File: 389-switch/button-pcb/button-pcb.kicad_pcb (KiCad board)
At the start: 2 copper layers, 17.4 x 17.4 mm, 6 parts, among them J1 Conn_01x04, SW1 SW_DIP_x01

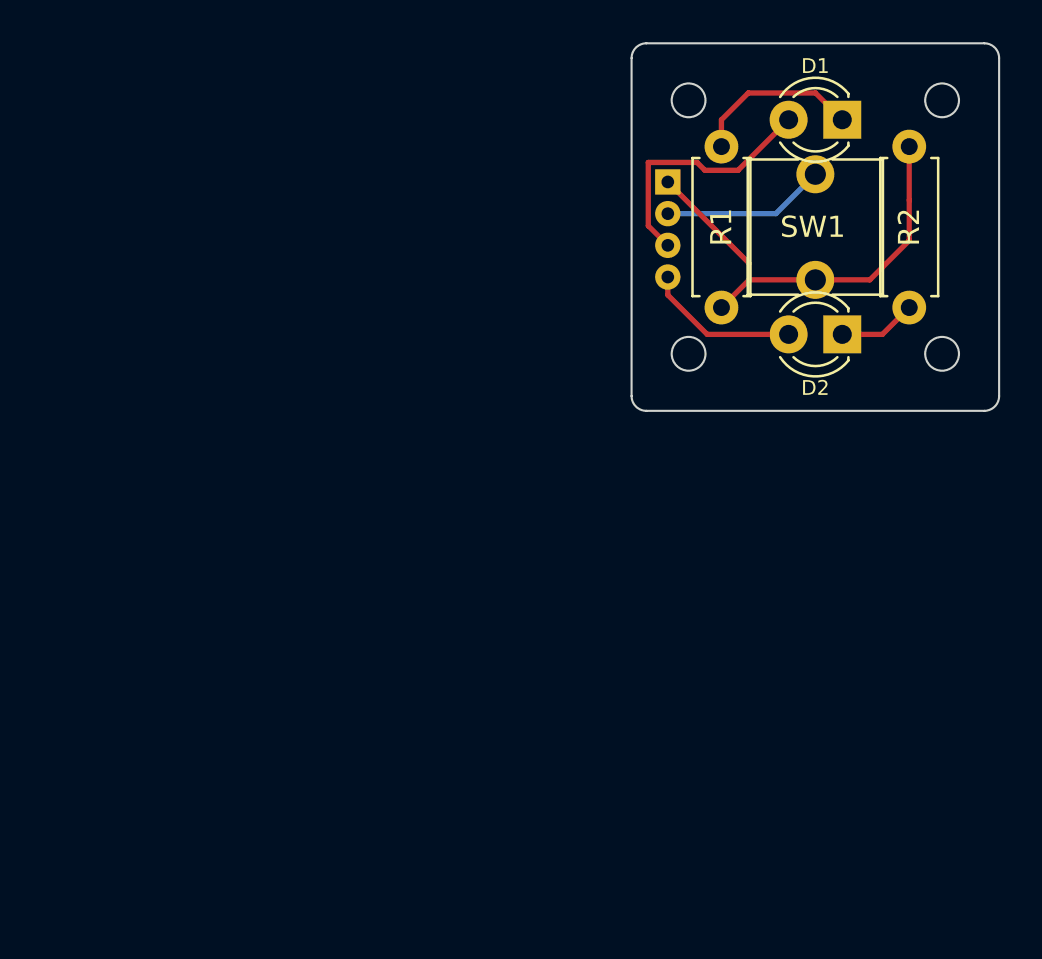
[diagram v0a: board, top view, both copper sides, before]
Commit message: changing pcb and creating gerber files
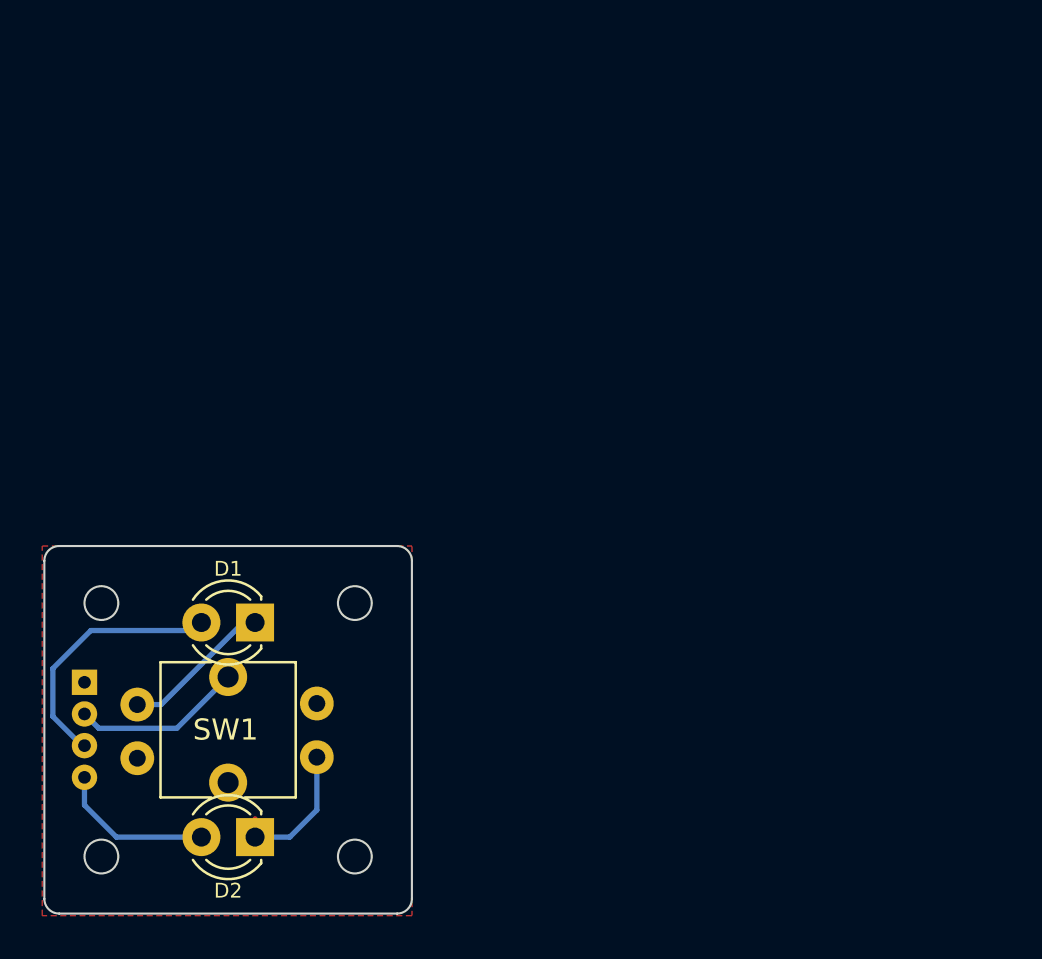
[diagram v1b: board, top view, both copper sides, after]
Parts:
- R1, R2: footprint Resistor_THT:R_Axial_DIN0207_L6.3mm_D2.5mm_P7.62mm_Horizontal -> Resistor_THT:R_Axial_DIN0207_L6.3mm_D2.5mm_P2.54mm_Vertical; moved to B.Cu
- moved R2 38.5 mm to (154.2, 98.8)
- moved J1 38.3 mm to (143.2, 100.0)
- moved SW1 36.6 mm to (150.0, 100.0)
- moved D1 36.6 mm to (151.3, 94.9)
- moved D2 36.6 mm to (151.3, 105.1)
- moved R1 34.9 mm to (145.7, 101.3)
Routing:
- net GND: track 20.9 -> 0.67 mm
- net Net-(D2-K): track 3.70 -> 6.82 mm
- net Net-(D1-K): track 8.04 -> 7.18 mm
- added copper zone on F.Cu, net GND

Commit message: adding controller board pcb
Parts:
- J1: footprint samuel:ZH-1.5mm-4p -> Connector_JST:JST_ZH_B4B-ZR_1x04_P1.50mm_Vertical
- moved J1 2.38 mm to (143.7, 102.3), turned to 90 degrees
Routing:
- net Net-(J1-Pin_2): track 8.18 -> 15.3 mm
- net Net-(D2-A): track 7.48 -> 13.6 mm
- net Net-(D1-A): track 12.3 -> 10.4 mm

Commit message: preparing for Production
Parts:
- R1, R2: footprint Resistor_THT:R_Axial_DIN0207_L6.3mm_D2.5mm_P2.54mm_Vertical -> Resistor_SMD:R_1206_3216Metric_Pad1.30x1.75mm_HandSolder; moved to F.Cu
- moved J1 4.55 mm to (143.2, 97.8), turned to -90 degrees
- moved R1 1.35 mm to (145.6, 100.0)
- moved R2 1.21 mm to (154.4, 100.0)
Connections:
- J1 pad 1: GND -> Net-(J1-Pin_1)
- J1 pad 2: Net-(J1-Pin_2) -> Net-(D1-A)
- J1 pad 3: Net-(D1-A) -> Net-(D2-A)
- J1 pad 4: Net-(D2-A) -> GND
- SW1 pad 2: Net-(J1-Pin_2) -> Net-(J1-Pin_1)
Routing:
- net Net-(J1-Pin_2): track 15.3 -> 0.00 mm
- net Net-(J1-Pin_1): track 0.00 -> 6.92 mm
- net Net-(D2-A): track 13.6 -> 8.35 mm
- net GND: track 0.67 -> 2.87 mm
- net Net-(D2-K): track 6.82 -> 5.73 mm
- net Net-(D1-A): track 10.4 -> 11.0 mm
- net Net-(D1-K): track 7.18 -> 7.70 mm
